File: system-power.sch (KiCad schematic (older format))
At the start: 38 parts, among them J1 Conn_01x02, J2 Conn_01x02, U1 MCP73831T-2ACI/OT, U2 BQ25504

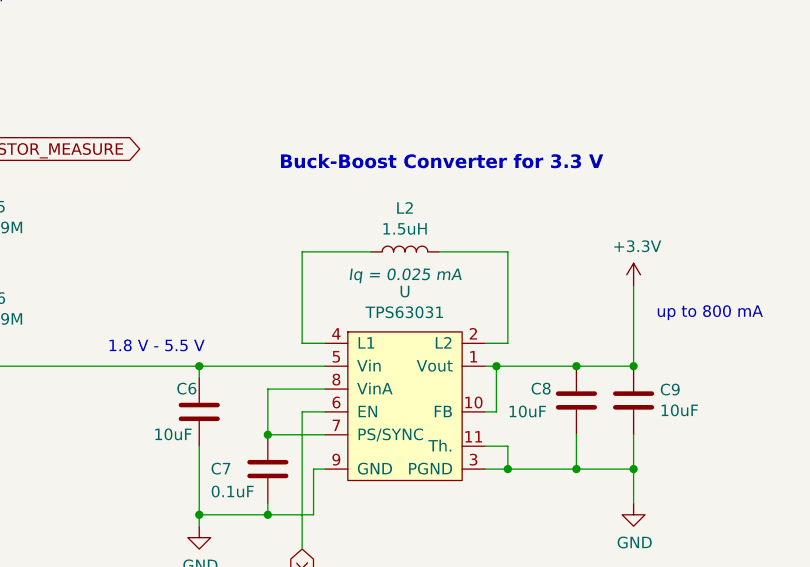
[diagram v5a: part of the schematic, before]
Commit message: Unnecessary note removed
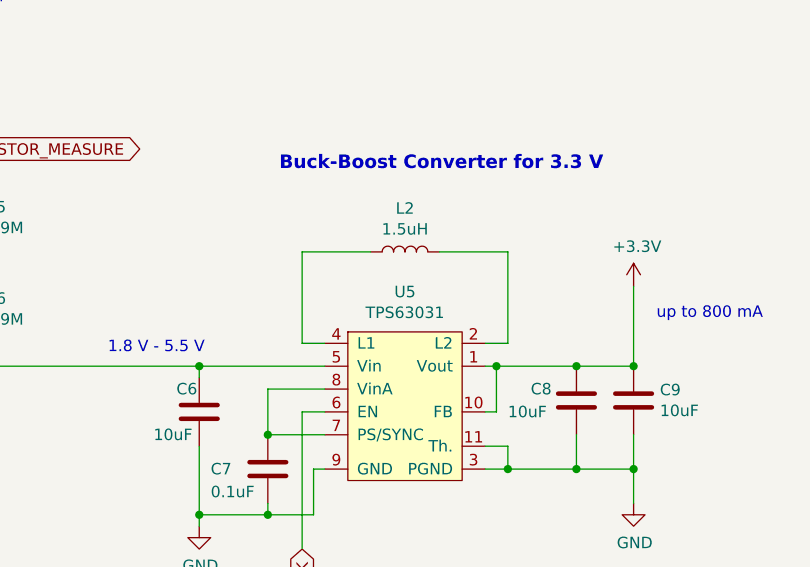
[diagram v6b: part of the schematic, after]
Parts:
- renumbered U to U5
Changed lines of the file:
@@
 $EndComp
 $Comp
-L tardigrade-components:TPS63031 U
+L tardigrade-components:TPS63031 U5
 U 1 1 5F6C19C3
 P 8700 3850
-F 0 "U" H 8700 4375 50  0000 C CNN
+F 0 "U5" H 8700 4375 50  0000 C CNN
 F 1 "TPS63031" H 8700 4284 50  0000 C CNN
 F 2 "tardigrade-components:TPS63031DSKR" H 8700 4050 50  0001 C CNN
 F 3 "https://www.ti.com/lit/ds/symlink/tps63031.pdf?ts=1600756672780&ref_url=https%253A%252F%252Fwww.ti.com%252Fproduct%252FTPS63031" H 8700 4050 50  0001 C CNN
-F 4 "Iq =  0.025 mA" H 8700 4450 50  0000 C CIN "Field4"
+F 4 "Iq =  0.025 mA" H 8700 4450 50  0001 C CIN "Field4"
 	1    8700 3850
 	1    0    0    -1
